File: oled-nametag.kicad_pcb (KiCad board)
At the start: 4 copper layers, 88 x 30 mm, 121 parts, among them J1 USB_C_Receptacle_USB2.0, J2 I2C, J3 LOAD, Q1 AO3401A, Q2 AO3401A, Q3 FS8205A, Q6 2N7002, SW1 Power, SW2 BTN1, SW3 BTN2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

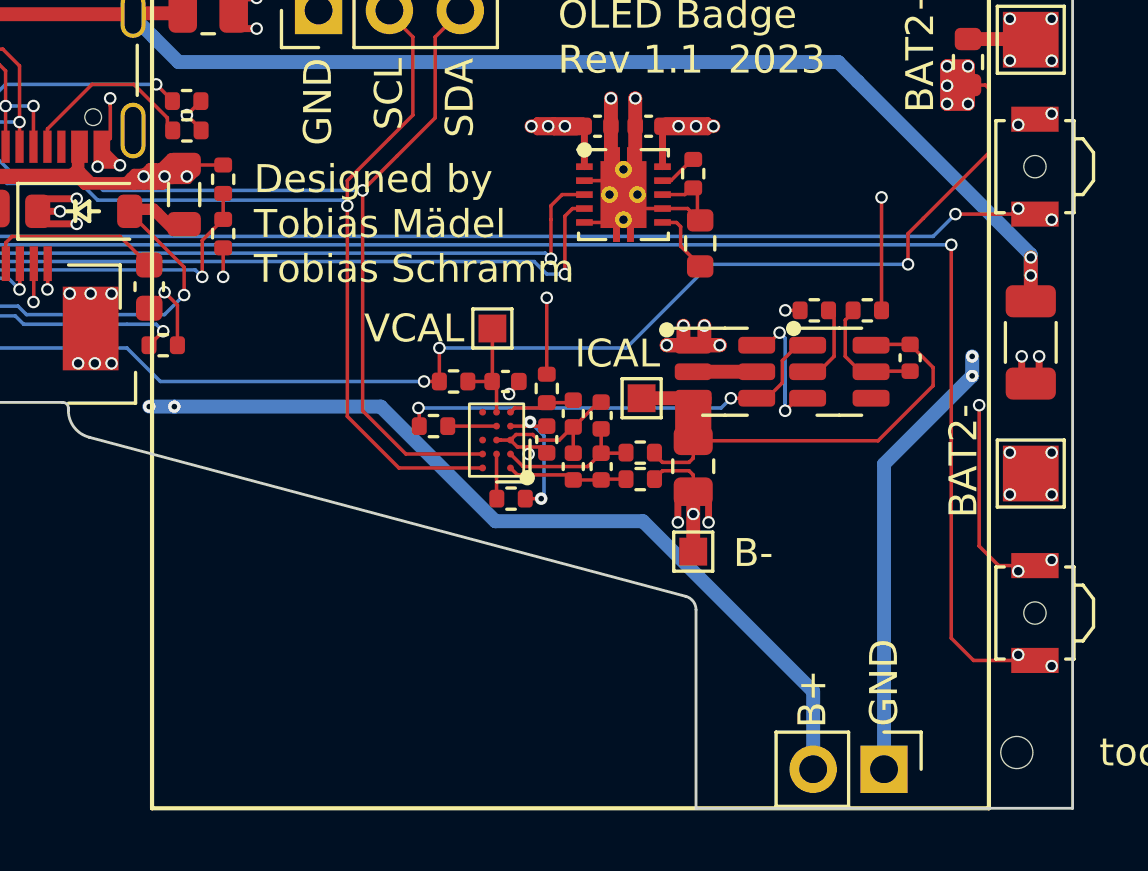
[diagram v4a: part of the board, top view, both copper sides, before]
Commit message: Add second light sensor position for reversed device mounting
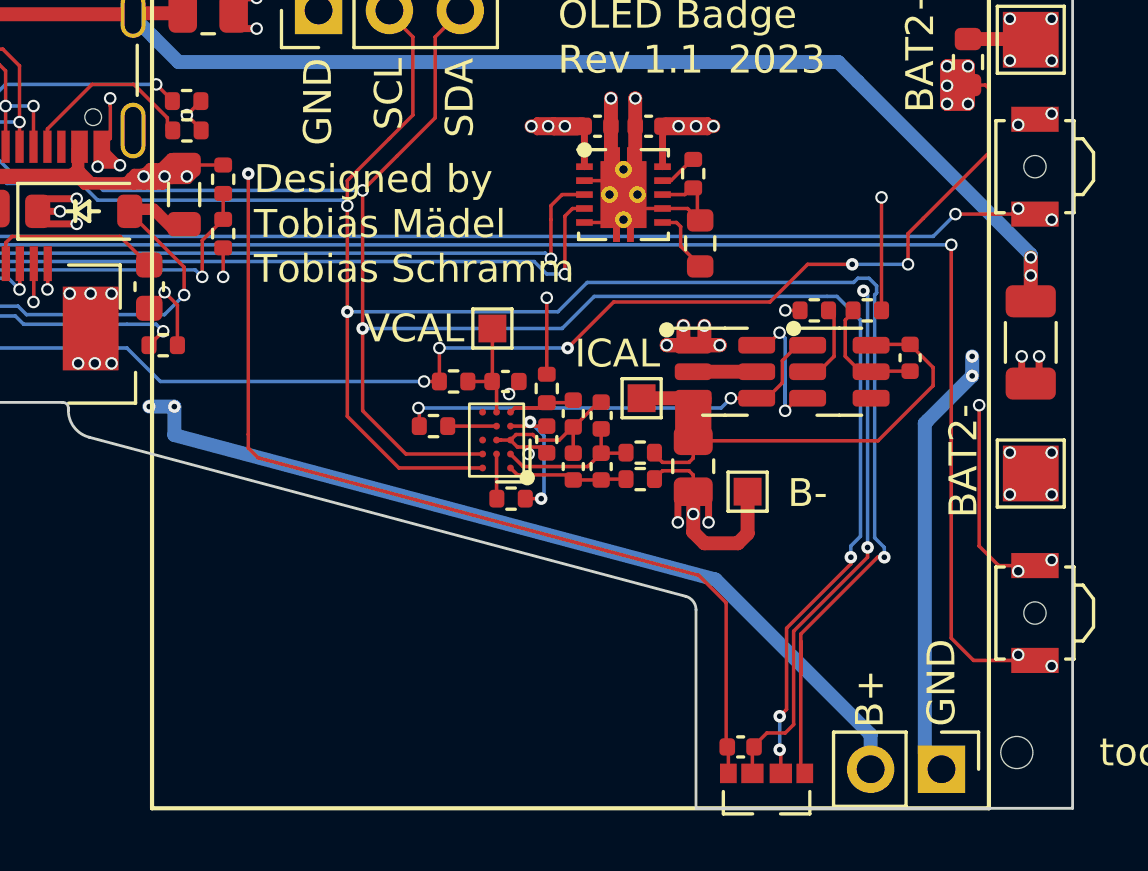
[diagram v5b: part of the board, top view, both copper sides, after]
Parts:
- added C41: 100nF, Capacitor_SMD:C_0402_1005Metric, F.Cu at (96.1, 47.8)
- added U13: ~, Sensor_Vishay:VEML3235SL, F.Cu at (97.0, 49.4)
- moved TP6 2.90 mm to (96.3, 38.6)
- moved J3 2.06 mm to (103.3, 48.6)
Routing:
- net /ESP32/SCL: track 78.5 -> 118.4 mm, vias 4 -> 6
- net /ESP32/SDA: track 76.1 -> 112.2 mm, vias 4 -> 8
- net +3V3: track 57.3 -> 92.8 mm, vias 22 -> 23
- net GND: track 180.5 -> 199.9 mm, vias 92 -> 94
- net GND1: track 15.4 -> 18.6 mm
- net +BATT: track 160.2 -> 160.5 mm, vias 24 -> 26

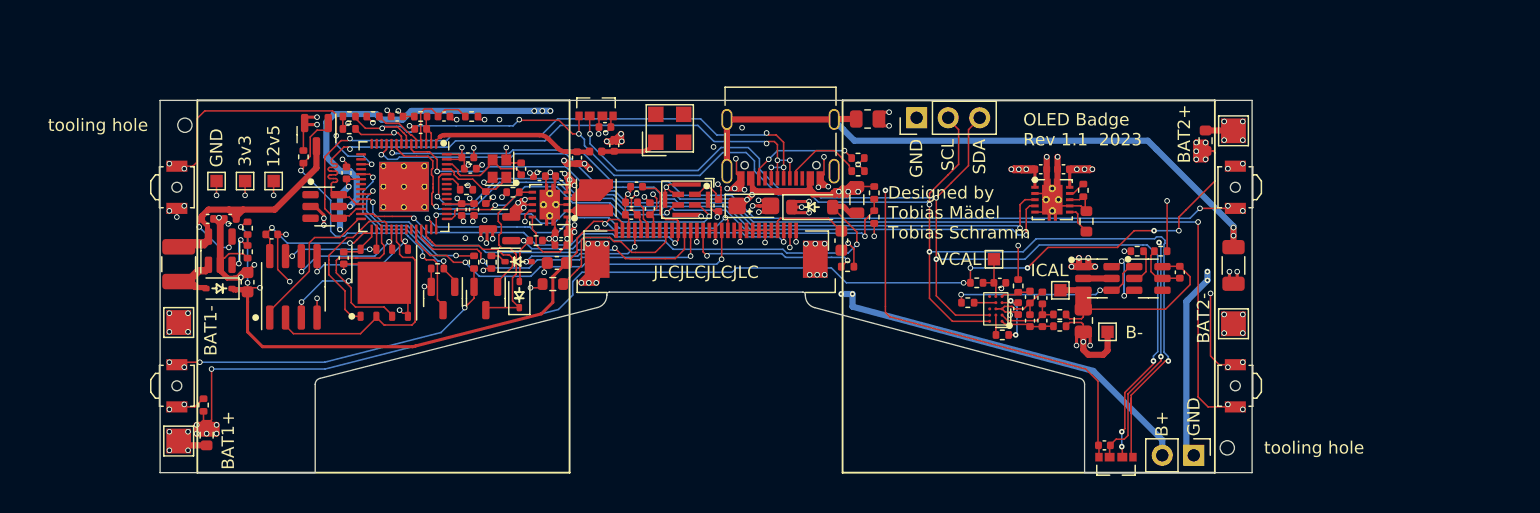
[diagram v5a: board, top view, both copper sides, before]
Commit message: Do rough component placement
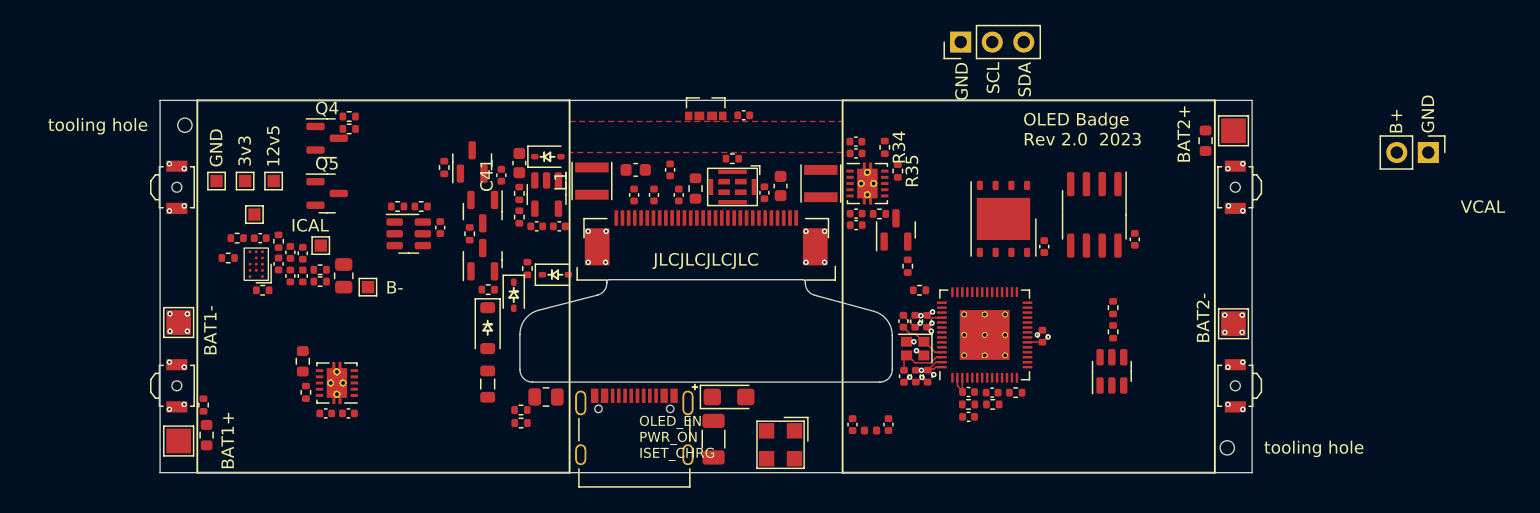
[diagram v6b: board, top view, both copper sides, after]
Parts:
- removed Q3: FS8205A, Package_TO_SOT_SMD:SOT-23-6
- removed U13: ~, Sensor_Vishay:VEML3235SL
- added Q4: AO3400A, Package_TO_SOT_SMD:SOT-23, F.Cu at (33.5, 23.1)
- added Q5: AO3400A, Package_TO_SOT_SMD:SOT-23, F.Cu at (33.5, 27.5)
- added R34: 0R, Resistor_SMD:R_0402_1005Metric, F.Cu at (78.4, 23.8)
- added R35: DNP, Resistor_SMD:R_0402_1005Metric, F.Cu at (79.5, 25.7)
- C41: value 100nF -> 22pF
- L1: footprint Inductor_SMD:L_1210_3225Metric -> Inductor_SMD:L_Taiyo-Yuden_MD-3030
- U7: value DW01+G -> FM2113
- moved C40 69.6 mm to (98.5, 31.2), turned to 90 degrees
- moved U9 64.8 mm to (96.7, 41.8), turned to 90 degrees
- moved U12 64.8 mm to (95.3, 29.2), turned to -90 degrees
- moved R15 64.7 mm to (31.8, 43.5), turned to 90 degrees
- moved R14 64.1 mm to (31.5, 41.0), turned to 90 degrees
- moved C27 62.6 mm to (33.4, 45.2), turned to 180 degrees
- moved C29 59.7 mm to (29.6, 33.2)
- moved R22 59.7 mm to (29.6, 31.4)
- moved R23 59.7 mm to (26.2, 31.1)
- moved R26 59.7 mm to (34.8, 34.1)
- moved R32 59.7 mm to (25.5, 32.7)
- moved R33 59.7 mm to (28.3, 35.3)
- moved C35 59.7 mm to (28.1, 31.1)
- moved R13 59.7 mm to (41.0, 28.6)
- moved R24 59.7 mm to (32.9, 33.6)
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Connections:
- C41 pad 1: GND -> Net-(U6-FB)
- C41 pad 2: +3V3 -> VCC
- U1 pad MR: GND1 -> GND
- U11 pad 10: +3V3 -> Net-(U11-FB)
- U3 pad 24: /ESP32/OLED_CS -> unconnected-(U3-GPIO18-Pad24)
- U3 pad 27: /ESP32/OLED_RST -> unconnected-(U3-GPIO21-Pad27)
- U3 pad 39: /ESP32/OLED_DC -> unconnected-(U3-GPIO34-Pad39)
- U3 pad 41: /ESP32/OLED_DATA -> /ESP32/OLED_DC
- U3 pad 42: /ESP32/PDM_DATA -> /ESP32/OLED_CS
- U3 pad 43: /ESP32/PDM_CLK -> /ESP32/OLED_RST
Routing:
- net Net-(D3-K): track 211.4 -> 0.00 mm, vias 13 -> 0
- net GND: track 199.9 -> 7.34 mm, vias 94 -> 22
- net +BATT: track 160.5 -> 0.00 mm, vias 26 -> 0
- net VBUS: track 124.7 -> 0.00 mm, vias 12 -> 0
- net /ESP32/SCL: track 118.4 -> 0.00 mm, vias 6 -> 0
- net /ESP32/SDA: track 112.2 -> 0.00 mm, vias 8 -> 0
- net /ESP32/~{BTN2}: track 87.1 -> 0.00 mm, vias 4 -> 2
- net +3V3: track 92.8 -> 8.70 mm, vias 23 -> 5
- net VCC: track 76.0 -> 0.00 mm, vias 6 -> 0
- net /ESP32/~{BTN3}: track 72.5 -> 0.00 mm, vias 4 -> 2
- net Net-(J1-SHIELD): track 56.9 -> 0.00 mm, vias 2 -> 0
- net /ESP32/~{CHRG}: track 56.7 -> 0.00 mm, vias 2 -> 0
- net /ESP32/~{STAT2}: track 56.0 -> 0.00 mm, vias 2 -> 0
- net /ESP32/D+: track 51.2 -> 0.00 mm, vias 4 -> 0
- net /ESP32/D-: track 50.8 -> 0.00 mm, vias 4 -> 0
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- added copper zone on F.Cu, net GND
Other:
- outline, holes or cut-outs redrawn
- board text added: "CHRG STAT2 USB"
- board text added: "OLED Badge Rev 2.0 2023"
- board text added: "OLED_EN PWR_ON ISET_CHRG"
- board text removed: "Designed by Tobias Mädel Tobias Schramm"
- board text removed: "OLED Badge Rev 1.1 2023"

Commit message: Finsh first layout iteration
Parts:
- removed TP9: GND, TestPoint:TestPoint_Pad_1.0x1.0mm
- added C42: DNP, Capacitor_SMD:C_0402_1005Metric, F.Cu at (35.2, 36.1)
- added C43: 10uF 25V, Capacitor_SMD:C_0603_1608Metric, F.Cu at (70.6, 27.1)
- added C44: 100nF, Capacitor_SMD:C_0402_1005Metric, F.Cu at (79.5, 26.8)
- added D6: BAV70, Package_TO_SOT_SMD:SOT-23, F.Cu at (101.9, 30.1)
- added D7: 4148WS, Diode_SMD:D_SOD-323, F.Cu at (84.0, 28.3)
- added R36: DNP, Resistor_SMD:R_0402_1005Metric, F.Cu at (33.3, 37.1)
- added R37: DNP, Resistor_SMD:R_0402_1005Metric, F.Cu at (33.3, 36.1)
- added R38: DNP, Resistor_SMD:R_0402_1005Metric, F.Cu at (35.2, 37.1)
- added R39: 100R, Resistor_SMD:R_0402_1005Metric, F.Cu at (23.7, 28.0)
- added R40: 100R, Resistor_SMD:R_0402_1005Metric, F.Cu at (104.3, 45.7)
- added R41: 100R, Resistor_SMD:R_0402_1005Metric, F.Cu at (103.9, 25.5)
- added R42: 10k, Resistor_SMD:R_0402_1005Metric, F.Cu at (101.3, 32.3)
- added R43: 10k, Resistor_SMD:R_0402_1005Metric, F.Cu at (95.3, 47.5)
- added R44: 10k, Resistor_SMD:R_0402_1005Metric, F.Cu at (101.8, 45.7)
- TP1: footprint TestPoint:TestPoint_Pad_1.0x1.0mm -> TestPoint:TestPoint_Pad_1.5x1.5mm
- TP10, TP6: footprint TestPoint:TestPoint_Pad_1.0x1.0mm -> TestPoint:TestPoint_Pad_2.0x2.0mm
- moved J3 95.1 mm to (30.3, 48.7)
- moved R8 64.0 mm to (98.8, 29.3), turned to 90 degrees
- moved R9 62.6 mm to (97.5, 29.3), turned to 90 degrees
- moved TP8 54.8 mm to (81.6, 26.9)
- moved J2 38.3 mm to (103.2, 48.7), turned to -90 degrees
- moved TP7 30.4 mm to (59.5, 25.4)
- moved TP6 17.0 mm to (24.7, 23.1), turned to 180 degrees
- moved R33 14.3 mm to (33.7, 22.1), turned to 180 degrees
- moved R29 13.5 mm to (86.2, 45.5), turned to 180 degrees
- moved R26 13.3 mm to (27.2, 23.3), turned to -90 degrees
- moved R32 13.3 mm to (36.0, 24.6), turned to 90 degrees
- moved R25 12.4 mm to (29.1, 22.8), turned to 0 degrees
- moved C25 12.1 mm to (31.0, 26.6), turned to 0 degrees
- moved R28 11.6 mm to (87.8, 46.0), turned to -135 degrees
- moved U10 11.1 mm to (34.2, 24.2), turned to 0 degrees
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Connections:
- net Net-(D4-K) renamed /Power/PWR_ON
- D4 pad 1: /ESP32/PWR_EN -> /ESP32/PWR_ON
- D4 pad 2: /ESP32/PWR_ON -> /ESP32/PWR_EN
- FB1 pad 1: VBUS -> Net-(D3-A)
- FB1 pad 2: Net-(D3-A) -> VBUS
- R29 pad 1: Net-(U3-GPIO17) -> Net-(U3-GPIO4)
- SW2 pad 1: GND -> Net-(R39-Pad2)
- SW3 pad 1: GND -> /ESP32/~{BTN2}
- SW3 pad 2: /ESP32/~{BTN2} -> Net-(R40-Pad2)
- SW4 pad 1: GND -> Net-(R41-Pad2)
- U3 pad 10: /ESP32/~{BTN3} -> /ESP32/USB_DET
- U3 pad 11: /ESP32/~{BTN2} -> unconnected-(U3-GPIO6-Pad11)
- U3 pad 15: unconnected-(U3-GPIO10-Pad15) -> /ESP32/SCL
- U3 pad 16: unconnected-(U3-GPIO11-Pad16) -> /ESP32/SDA
- U3 pad 17: /ESP32/~{BTN1} -> Net-(U3-GPIO12)
- U3 pad 18: unconnected-(U3-GPIO13-Pad18) -> Net-(U3-GPIO13)
- U3 pad 19: /ESP32/OLED_EN -> Net-(U3-GPIO14)
- U3 pad 23: Net-(U3-GPIO17) -> /ESP32/OLED_RST
- U3 pad 24: unconnected-(U3-GPIO18-Pad24) -> /ESP32/OLED_EN
- U3 pad 27: unconnected-(U3-GPIO21-Pad27) -> /ESP32/PWR_EN
- U3 pad 38: /ESP32/OLED_CLK -> /ESP32/PDM_DATA
- U3 pad 39: unconnected-(U3-GPIO34-Pad39) -> /ESP32/PDM_CLK
- U3 pad 40: /ESP32/PWR_EN -> /ESP32/OLED_DATA
- U3 pad 41: /ESP32/OLED_DC -> /ESP32/OLED_CLK
- U3 pad 42: /ESP32/OLED_CS -> /ESP32/OLED_DC
- U3 pad 43: /ESP32/OLED_RST -> /ESP32/OLED_CS
- U3 pad 52: /ESP32/~{STAT2} -> /ESP32/CHRG_PWM
- U3 pad 6: /ESP32/~{CHRG} -> unconnected-(U3-GPIO1-Pad6)
- U3 pad 7: /ESP32/SCL -> /ESP32/~{STAT2}
- U3 pad 8: /ESP32/SDA -> /ESP32/~{CHRG}
- U3 pad 9: /ESP32/USB_DET -> Net-(U3-GPIO4)
- U9 pad 1: unconnected-(U9-IO1-Pad1) -> /ESP32/D+
- U9 pad 3: unconnected-(U9-IO2-Pad3) -> /ESP32/D-
- U9 pad 4: /ESP32/D+ -> unconnected-(U9-IO3-Pad4)
- U9 pad 6: /ESP32/D- -> unconnected-(U9-IO4-Pad6)
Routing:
- net +BATT: track 0.00 -> 194.0 mm, vias 0 -> 17
- net VBUS: track 0.00 -> 151.9 mm, vias 0 -> 12
- net /ESP32/SCL: track 0.00 -> 123.7 mm, vias 0 -> 5
- net /ESP32/SDA: track 0.00 -> 122.8 mm, vias 0 -> 4
- net GND: track 7.34 -> 123.4 mm, vias 22 -> 93
- net Net-(D3-K): track 0.00 -> 111.9 mm, vias 0 -> 9
- net /ESP32/PWR_ON: track 0.00 -> 111.7 mm, vias 2 -> 9
- net /ESP32/~{BTN1}: track 0.00 -> 100.4 mm, vias 2 -> 6
- net /Power/PWR_ON: track 0.00 -> 65.7 mm, vias 0 -> 5
- net /ESP32/~{CHRG}: track 0.00 -> 60.0 mm, vias 0 -> 3
- net /ESP32/~{STAT2}: track 0.00 -> 59.6 mm, vias 0 -> 3
- net /ESP32/CHRG_PWM: track 0.00 -> 59.3 mm, vias 0 -> 4
- net /ESP32/D+: track 0.00 -> 52.8 mm, vias 0 -> 2
- net /ESP32/D-: track 0.00 -> 50.3 mm, vias 0 -> 3
- net /ESP32/OLED_EN: track 0.00 -> 49.0 mm, vias 0 -> 2
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- added copper zone on F.Cu, net Net-(D2-A)
- added copper zone on F.Cu, net Net-(U11-L1)
- added copper zone on F.Cu, net Net-(U11-L2)
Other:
- board text added: "ICAL+"
- board text removed: "B-"
- board text removed: "CHRG STAT2 USB"
- board text removed: "ICAL"
- board text removed: "OLED_EN PWR_ON ISET_CHRG"
